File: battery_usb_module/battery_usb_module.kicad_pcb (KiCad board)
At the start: 2 copper layers, 58.5 x 30.5 mm, 6 parts, among them J1 USB_C_Receptacle_USB2.0_16P, J2 DF12NC_3.0_-60DS-0.5V_51_, J3 Conn_01x02_MountingPin, U1 LP3947

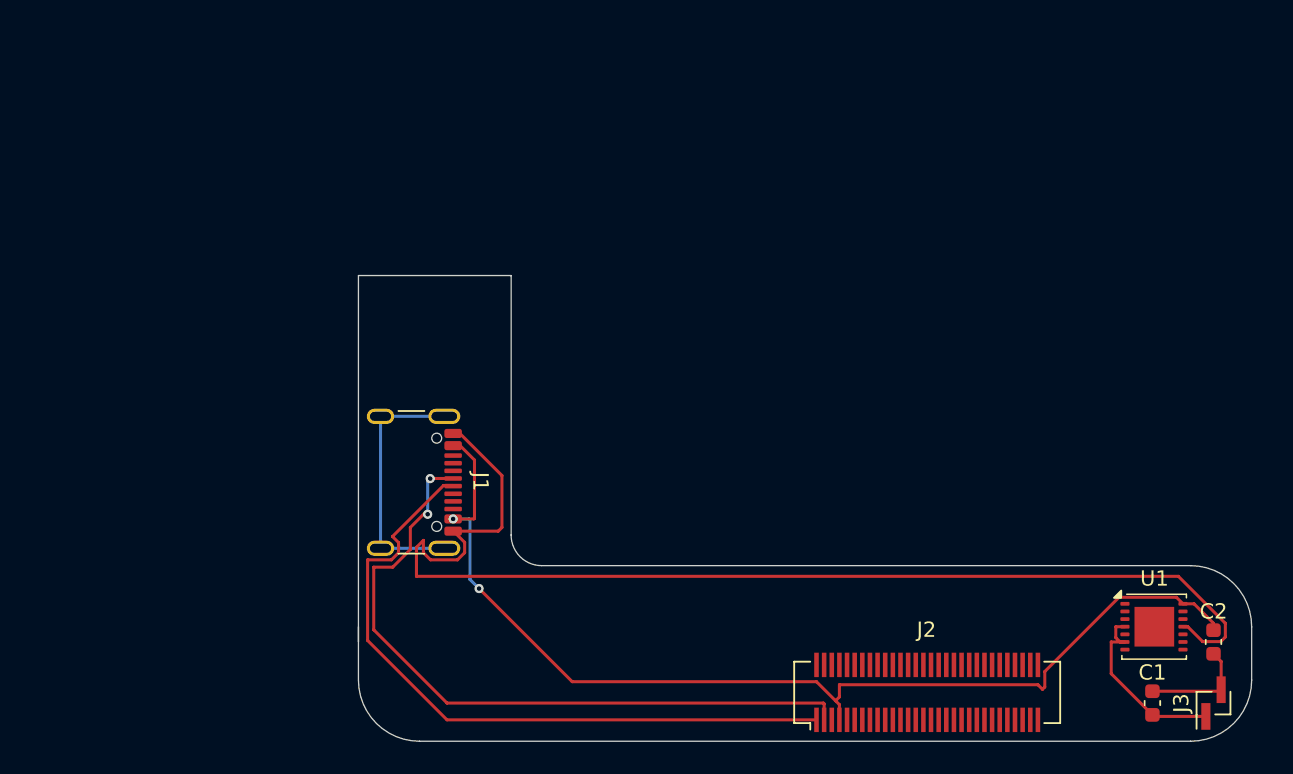
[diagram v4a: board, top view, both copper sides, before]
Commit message: Move connector in battery module ,new usb-c footprint and symbol in pcb and schematic, fixed wrong capacitor values, and redid some wiring on battery module
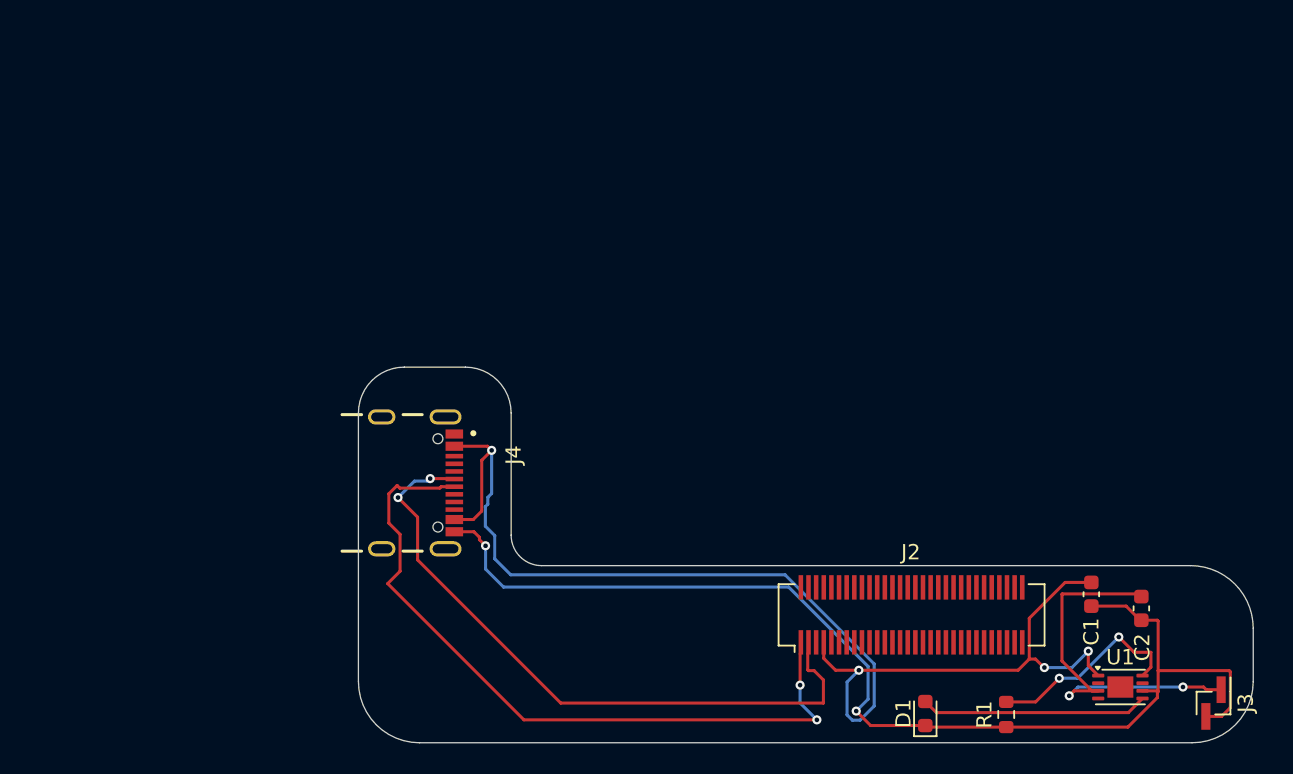
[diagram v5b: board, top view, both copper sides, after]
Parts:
- removed J1: USB_C_Receptacle_USB2.0_16P, Connector_USB:USB_C_Receptacle_GCT_USB4105-xx-A_16P_TopMnt_Horizontal
- added D1: LED, LED_SMD:LED_0603_1608Metric, F.Cu at (173.1, 115.7)
- added J4: USB4105GFA120, USB4105GFA120:GCT_USB4105GFA120, F.Cu at (137.5, 100.6)
- added R1: 333Ω, Resistor_SMD:R_0603_1608Metric, F.Cu at (178.4, 115.8)
- C1: value 10uF -> 4.7uF
- C2: value 1uF -> 4.7uF
- U1: value LP3947 -> MCP73831-2-MC; footprint Package_SON:WSON-14-1EP_4.0x4.0mm_P0.5mm_EP2.6x2.6mm -> Package_DFN_QFN:DFN-8-1EP_3x2mm_P0.5mm_EP1.7x1.4mm
- moved C1 8.17 mm to (184.0, 107.9), turned to 90 degrees
- moved C2 5.21 mm to (187.3, 108.8)
- moved J2 5.18 mm to (172.2, 109.2)
- moved U1 4.52 mm to (185.9, 114.0)
- turned J3 to -90 degrees
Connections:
- C1 pad 2: Net-(J3-Pin_1) -> Net-(C1-Pad2)
- C2 pad 2: Net-(U1-CHG_IN) -> Net-(J3-Pin_1)
- J2 pad 4: Net-(U1-CHG_IN) -> Net-(C1-Pad2)
- U1 pad 1: unconnected-(U1-EN-Pad1) -> Net-(C1-Pad2)
- U1 pad 2: unconnected-(U1-SCL-Pad2) -> Net-(C1-Pad2)
- U1 pad 3: unconnected-(U1-SDA-Pad3) -> Net-(J3-Pin_1)
- U1 pad 5: unconnected-(U1-V_{T}-Pad5) -> Net-(D1-A)
- U1 pad 6: Net-(J3-Pin_1) -> GND
- U1 pad 8: unconnected-(U1-DIFF_AMP-Pad8) -> Net-(U1-PROG)
- U1 pad 9: unconnected-(U1-Ts-Pad9) -> (no net)
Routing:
- net Net-(C1-Pad2): track 0.00 -> 81.6 mm, vias 0 -> 4
- net Net-(U1-GND): track 77.7 -> 0.00 mm
- net Net-(U1-CHG_IN): track 70.7 -> 0.00 mm, vias 2 -> 0
- net GND: track 7.10 -> 75.8 mm, vias 0 -> 2
- net unconnected-(J1-SHIELD-PadS1): track 17.0 -> 0.00 mm
- net Net-(D1-A): track 0.00 -> 14.9 mm
- net Net-(U1-PROG): track 0.00 -> 13.4 mm, vias 0 -> 2
- net Net-(J3-Pin_1): track 12.4 -> 25.3 mm, vias 0 -> 2
- net Net-(J4-DP1): track 46.5 -> 43.3 mm
- net Net-(J4-DN1): track 45.6 -> 47.7 mm, vias 0 -> 2
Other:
- board size 58.5 x 30.5 mm -> 58.6 x 24.6 mm

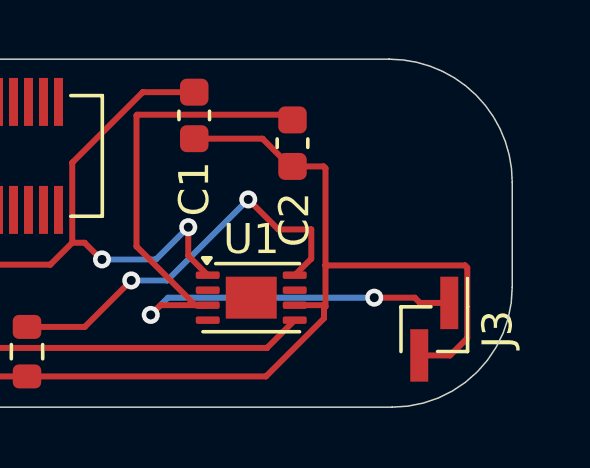
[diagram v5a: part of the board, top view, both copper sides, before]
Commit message: Change pin headers on battery usb module to throughhole
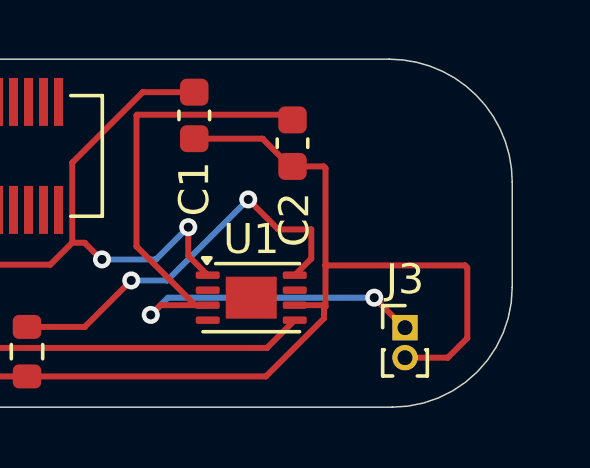
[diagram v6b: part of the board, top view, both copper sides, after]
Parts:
- J3: footprint Connector_PinHeader_1.00mm:PinHeader_1x02_P1.00mm_Vertical_SMD_Pin1Left -> Connector_PinHeader_1.00mm:PinHeader_1x02_P1.00mm_Vertical
- moved J3 0.98 mm to (191.0, 115.0), turned to 0 degrees
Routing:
- net Net-(J3-Pin_1): track 25.3 -> 24.0 mm
- net GND: track 75.8 -> 76.3 mm
